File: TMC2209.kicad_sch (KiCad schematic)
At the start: 26 parts, among them J11 Stepper, U7 TMC2209-LA

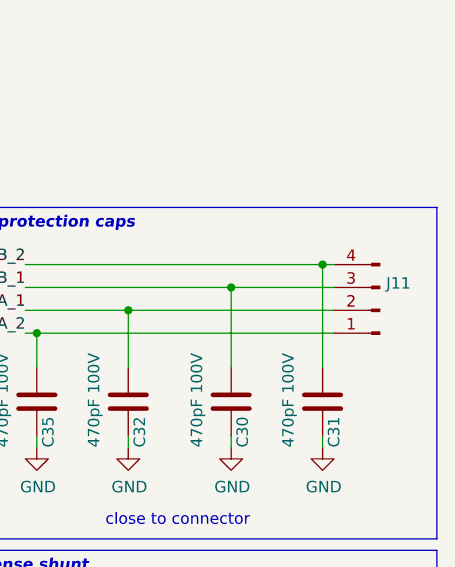
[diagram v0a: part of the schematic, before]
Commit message: Apply suggestions from tux: Single connector for signals Some (better) notes
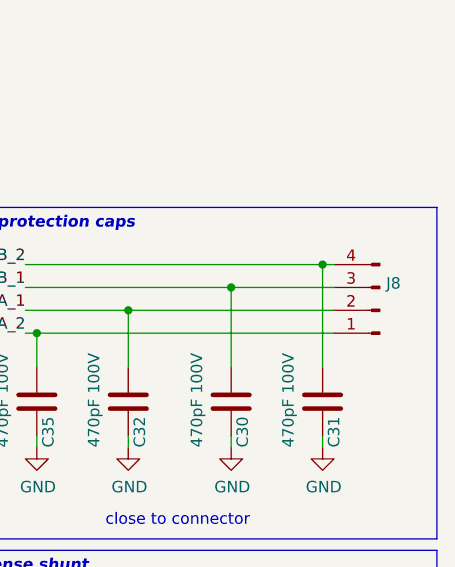
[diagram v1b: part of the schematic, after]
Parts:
- renumbered J11 to J8
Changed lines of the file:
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@@
   (symbol (lib_id "Connector:Conn_01x04_Male") (at 276.86 86.36 180) (unit 1)
     (in_bom yes) (on_board yes)
-    (property "Reference" "J11" (id 0) (at 277.5712 83.3628 0)
+    (property "Reference" "J8" (id 0) (at 277.5712 83.3628 0)
       (effects (font (size 1.27 1.27)) (justify right))
     )
